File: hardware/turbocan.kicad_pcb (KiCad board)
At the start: 2 copper layers, 43 x 43 mm, 86 parts, among them J1 USB_C_Receptacle_USB2.0, J10 CAN_PORT, J11 FAN0, J12 FAN1, J13 HEAT, J14 PROBE, J2 STEPPER, J5 DEBUG, J7 ENDSTOPX, J8 ENDSTOPY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

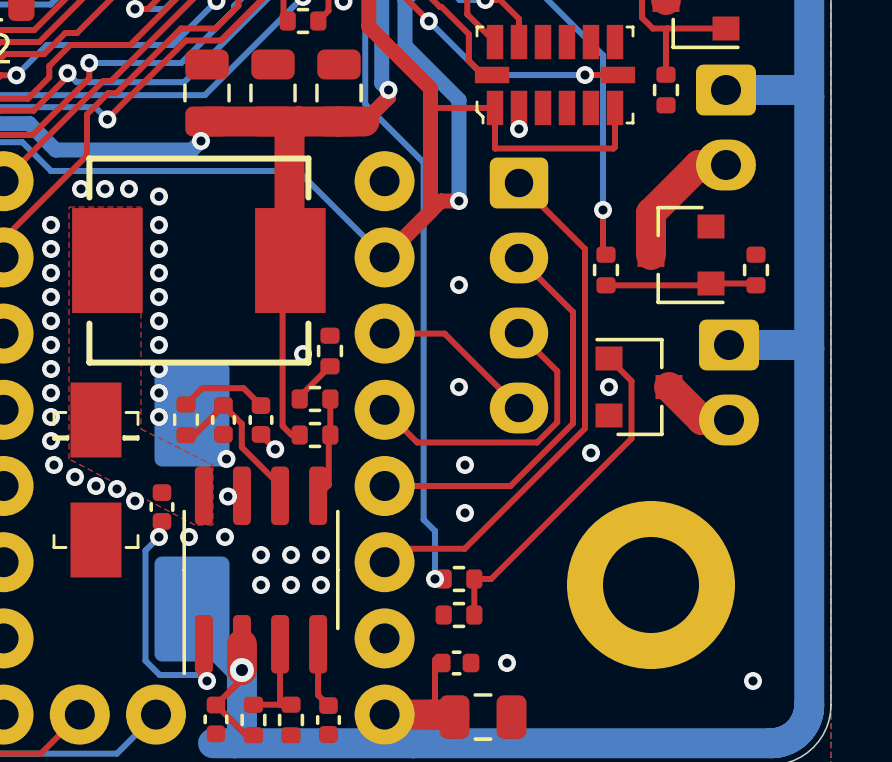
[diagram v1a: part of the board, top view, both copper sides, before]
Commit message: Replace heater mosfet
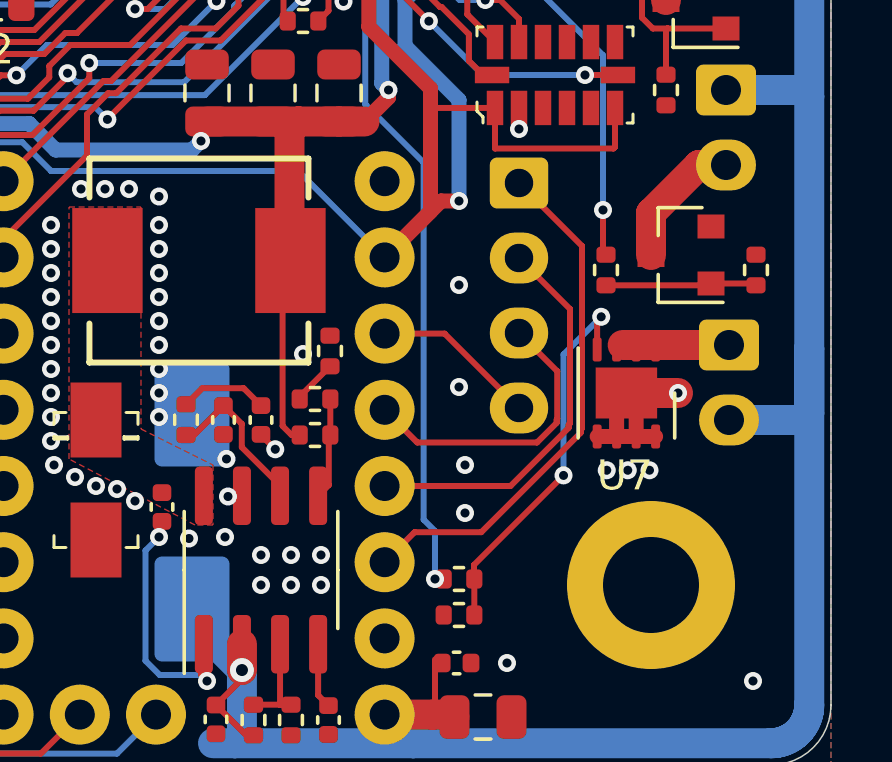
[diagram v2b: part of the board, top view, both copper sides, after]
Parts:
- U7: value AO3400A -> AON7400A; footprint Package_TO_SOT_SMD:SOT-23 -> turbocan:DFN-8-1EP_3x3mm_P0.65mm_EP1.7x2.05mm
- moved U7 0.47 mm to (50.2, 44.6), turned to 270 degrees
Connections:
- J1 pad A8: Net-(J1-PadA8) -> (no net)
- J1 pad B8: Net-(J1-PadB8) -> (no net)
- J13 pad 1: +24V -> Net-(J13-Pad1)
- J13 pad 2: Net-(J13-Pad2) -> +24V
- U3 pad 5: Net-(U3-Pad5) -> (no net)
- U7 pad 1: Net-(R16-Pad1) -> Net-(J13-Pad1)
- U7 pad 2: GND -> Net-(R16-Pad1)
- U7 pad 3: Net-(J13-Pad2) -> GND
- U8 pad 18: Net-(U8-Pad18) -> (no net)
- U8 pad 2: Net-(U8-Pad2) -> (no net)
- U8 pad 21: Net-(U8-Pad21) -> (no net)
- U8 pad 3: Net-(U8-Pad3) -> (no net)
- U8 pad 38: Net-(U8-Pad38) -> (no net)
- U8 pad 39: Net-(U8-Pad39) -> (no net)
- U8 pad 4: Net-(U8-Pad4) -> (no net)
- U9 pad 10: Net-(U9-Pad10) -> (no net)
- U9 pad 11: Net-(U9-Pad11) -> (no net)
- U9 pad 3: Net-(U9-Pad3) -> (no net)
- U9 pad 8: Net-(U9-Pad8) -> (no net)
- U9 pad 9: Net-(U9-Pad9) -> (no net)
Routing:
- net GND: track 28.0 -> 34.9 mm, vias 74 -> 76
- net Net-(J13-Pad1): track 0.00 -> 3.54 mm
- net Net-(J13-Pad2): track 2.46 -> 0.00 mm
- net +24V: track 185.1 -> 187.6 mm
- net Net-(R16-Pad1): track 11.4 -> 12.8 mm, vias 0 -> 2

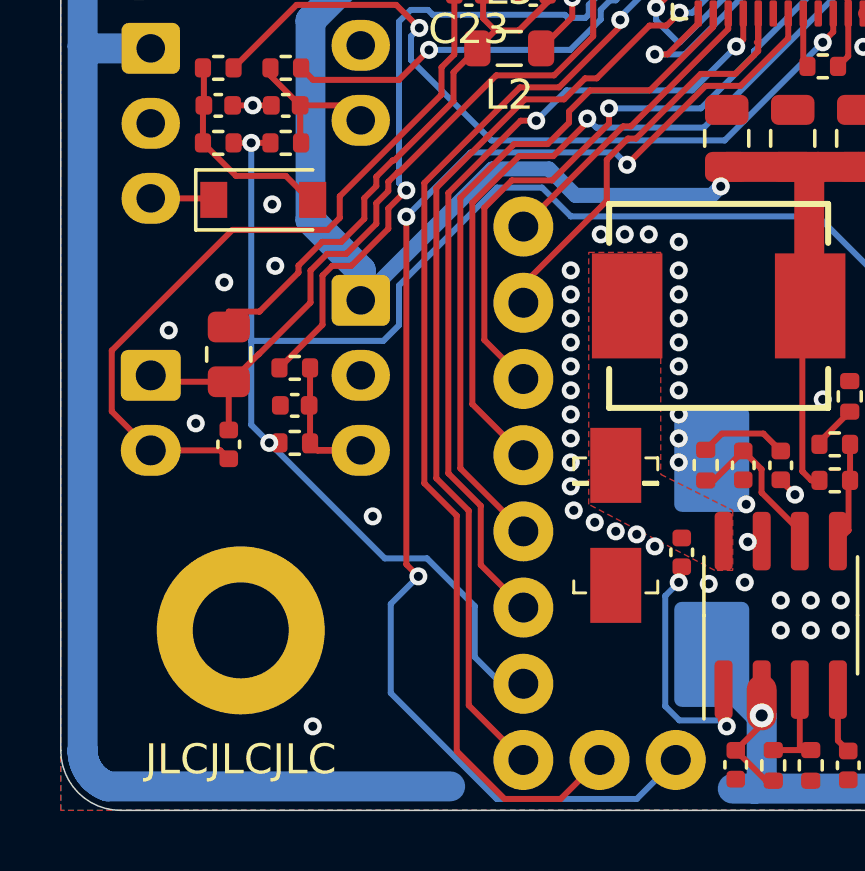
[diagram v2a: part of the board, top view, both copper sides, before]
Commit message: Replace pullup on MS1 with unpopulated resistor
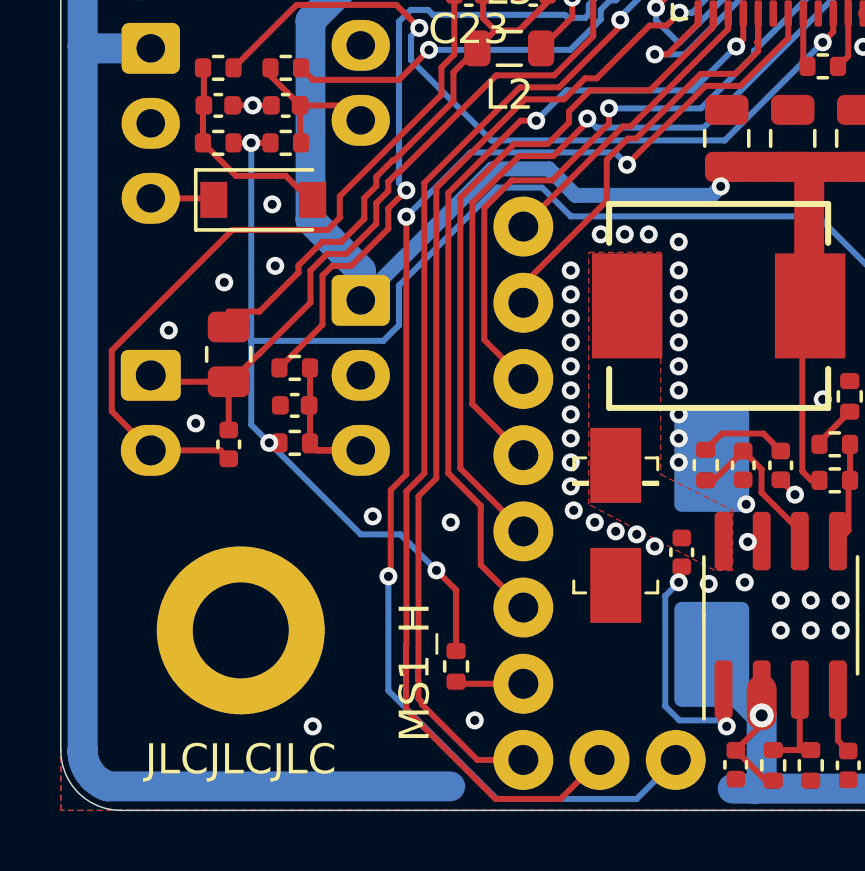
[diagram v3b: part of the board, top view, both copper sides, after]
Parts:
- added R29: DNP, Resistor_SMD:R_0402_1005Metric, F.Cu at (27.2, 52.2)
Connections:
- J1 pad A8: (no net) -> Net-(J1-PadA8)
- J1 pad B8: (no net) -> Net-(J1-PadB8)
- U2 pad 15: +3V3 -> Net-(R29-Pad2)
- U3 pad 5: (no net) -> Net-(U3-Pad5)
- U8 pad 18: (no net) -> Net-(U8-Pad18)
- U8 pad 2: (no net) -> Net-(U8-Pad2)
- U8 pad 21: (no net) -> Net-(U8-Pad21)
- U8 pad 3: (no net) -> Net-(U8-Pad3)
- U8 pad 38: (no net) -> Net-(U8-Pad38)
- U8 pad 39: (no net) -> Net-(U8-Pad39)
- U8 pad 4: (no net) -> Net-(U8-Pad4)
- U9 pad 10: (no net) -> Net-(U9-Pad10)
- U9 pad 11: (no net) -> Net-(U9-Pad11)
- U9 pad 3: (no net) -> Net-(U9-Pad3)
- U9 pad 8: (no net) -> Net-(U9-Pad8)
- U9 pad 9: (no net) -> Net-(U9-Pad9)
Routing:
- net +3V3: track 162.2 -> 159.7 mm, vias 13 -> 14
- net Net-(R29-Pad2): track 0.00 -> 2.27 mm
- net EN: track 41.9 -> 43.3 mm
- net DIAG: track 45.8 -> 46.5 mm
- net GND: vias 76 -> 78
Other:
- board text added: "MS1_H"

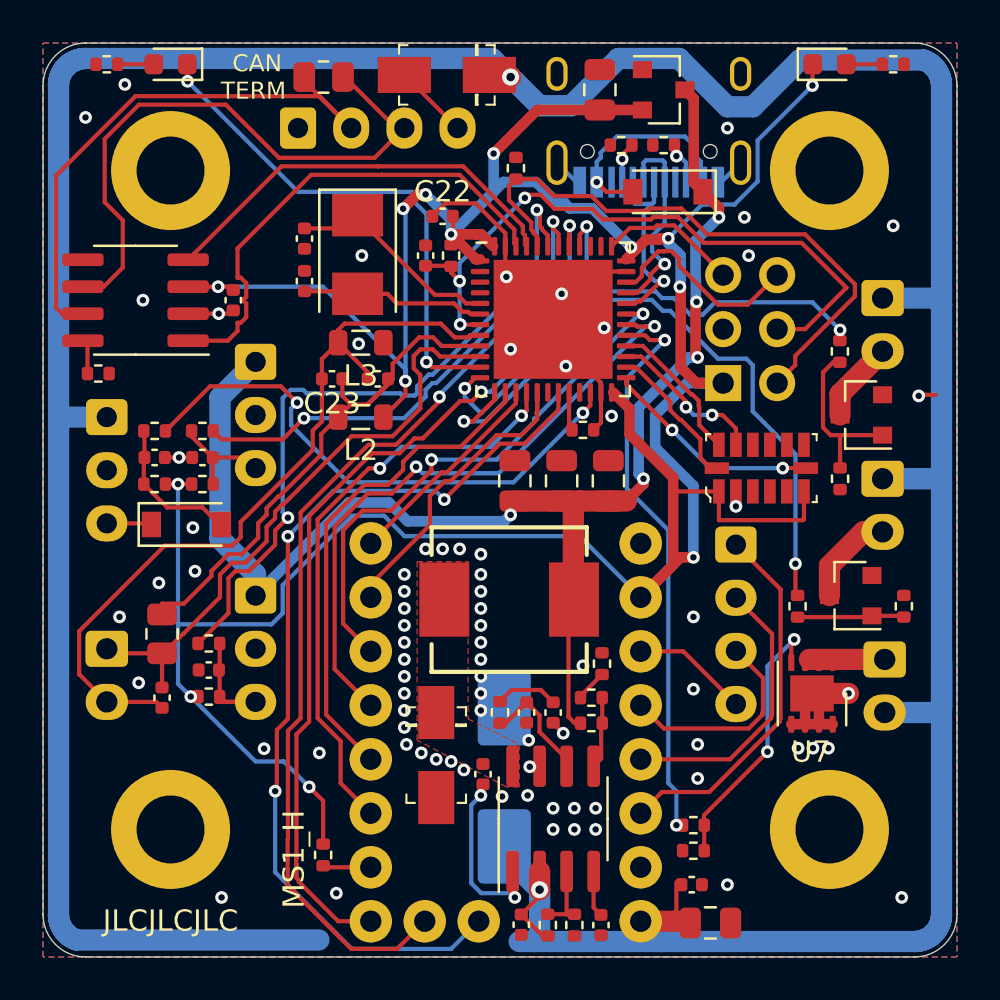
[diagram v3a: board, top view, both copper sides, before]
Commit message: Also add optional pullup resistors on MS2 and SPREAD
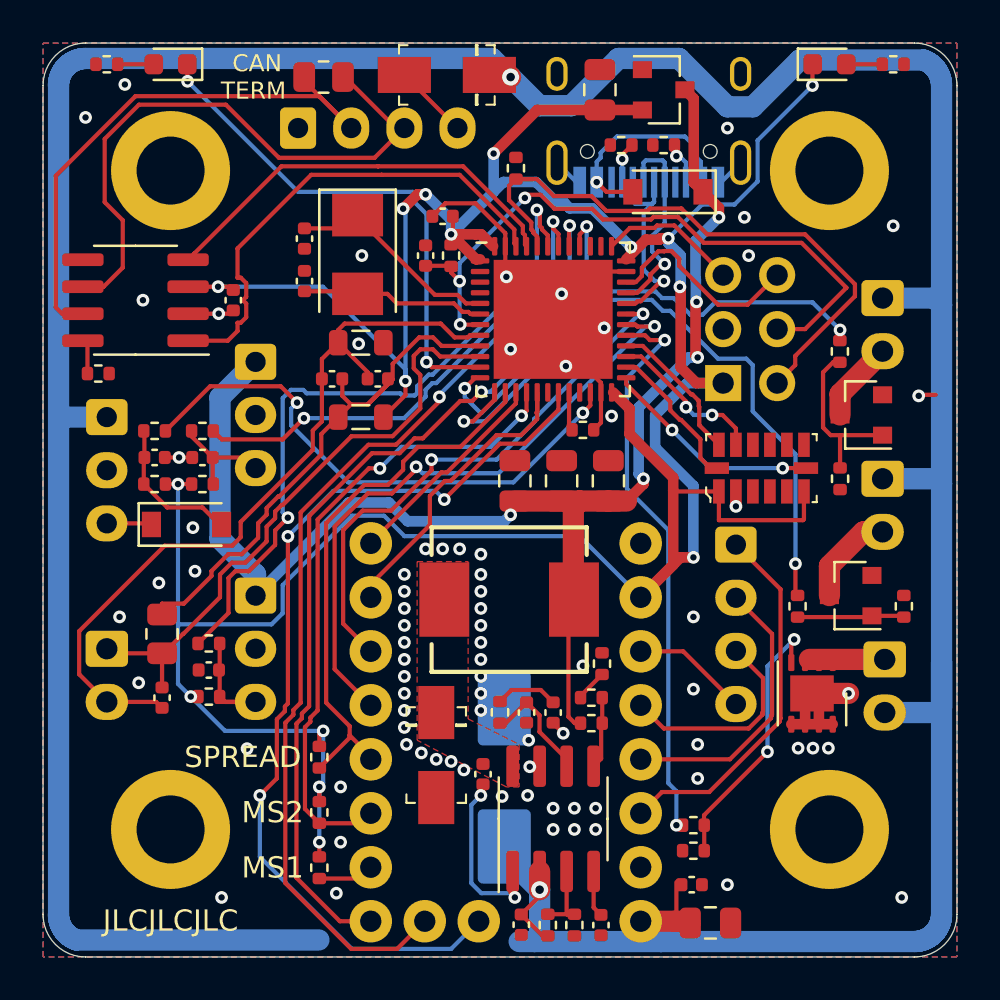
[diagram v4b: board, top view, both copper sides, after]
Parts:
- added R30: DNP, Resistor_SMD:R_0402_1005Metric, F.Cu at (27.0, 50.2)
- added R31: DNP, Resistor_SMD:R_0402_1005Metric, F.Cu at (27.0, 47.6)
- moved R29 0.63 mm to (27.0, 52.8)
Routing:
- net +3V3: track 159.7 -> 163.8 mm, vias 14 -> 16
- net MISO: track 27.7 -> 30.2 mm
- net INT2: track 23.4 -> 25.6 mm
- net INDEX: track 44.0 -> 44.6 mm
- net GND: vias 78 -> 79
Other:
- board text added: "MS1"
- board text added: "MS2"
- board text added: "SPREAD"
- board text removed: "MS1_H"

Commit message: Fix orientation of LEDs/C21 and update C8 to 1pF
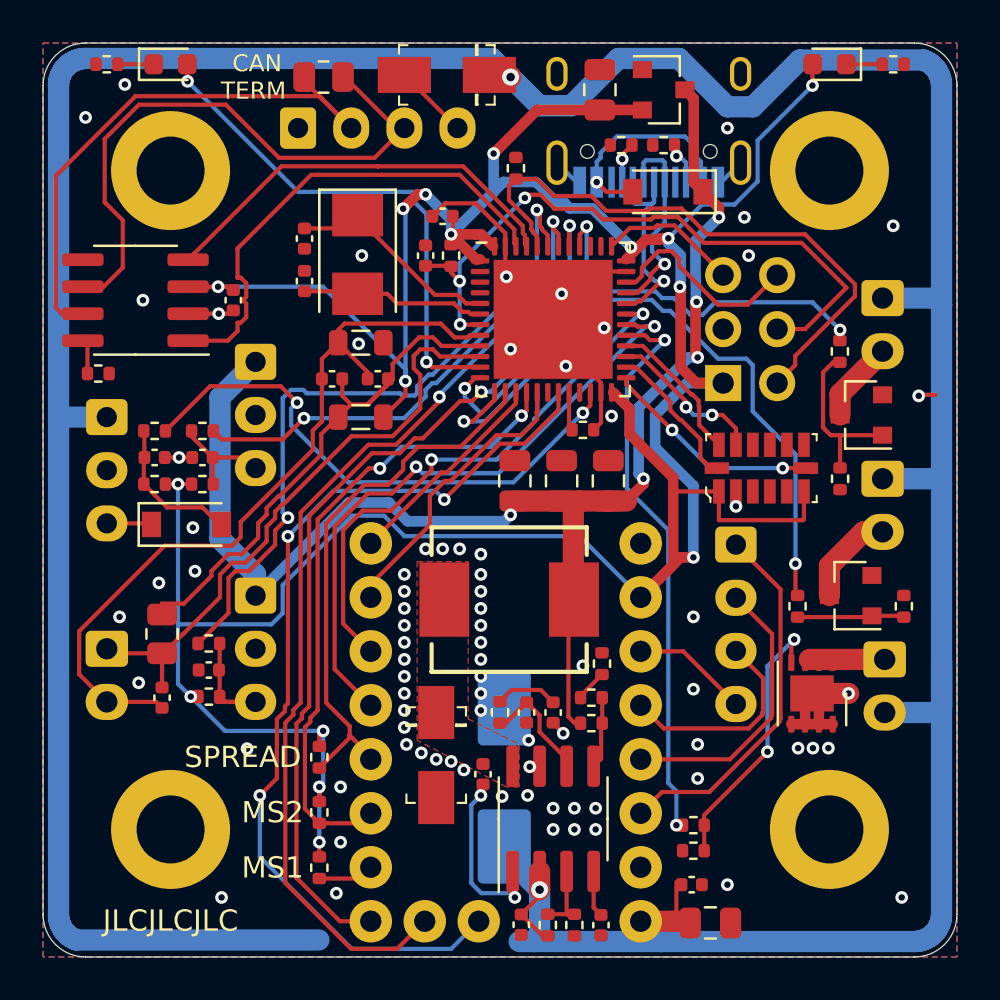
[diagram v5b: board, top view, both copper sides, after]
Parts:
- C8: value 6.8nF -> 1pF
- L1: value 10uH -> 6.8uH
- turned C21 to 90 degrees
- turned D5 to 0 degrees
- turned D6 to 180 degrees
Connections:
- C21 pad 1: GND -> +24V
- C21 pad 2: +24V -> GND
- D5 pad 1: LED -> Net-(D5-Pad1)
- D5 pad 2: Net-(D5-Pad2) -> LED
- D6 pad 1: +3V3 -> Net-(D6-Pad1)
- D6 pad 2: Net-(D6-Pad2) -> +3V3
- R23 pad 1: Net-(D5-Pad2) -> Net-(D5-Pad1)
- R24 pad 1: Net-(D6-Pad2) -> Net-(D6-Pad1)
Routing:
- net Net-(D6-Pad2): track 1.70 -> 0.00 mm
- net Net-(D6-Pad1): track 0.00 -> 1.70 mm
- net Net-(D5-Pad2): track 1.70 -> 0.00 mm
- net Net-(D5-Pad1): track 0.00 -> 1.70 mm

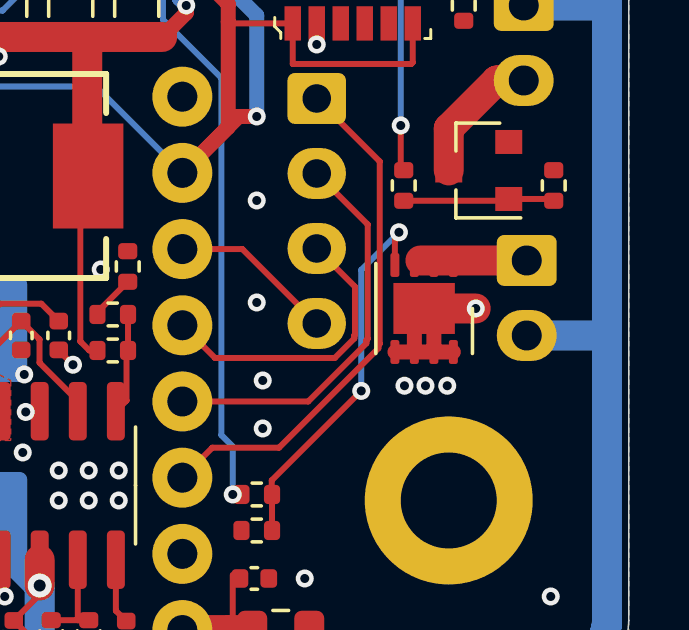
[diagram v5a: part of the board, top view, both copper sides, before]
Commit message: Swap drain and source on heater MOSFET.
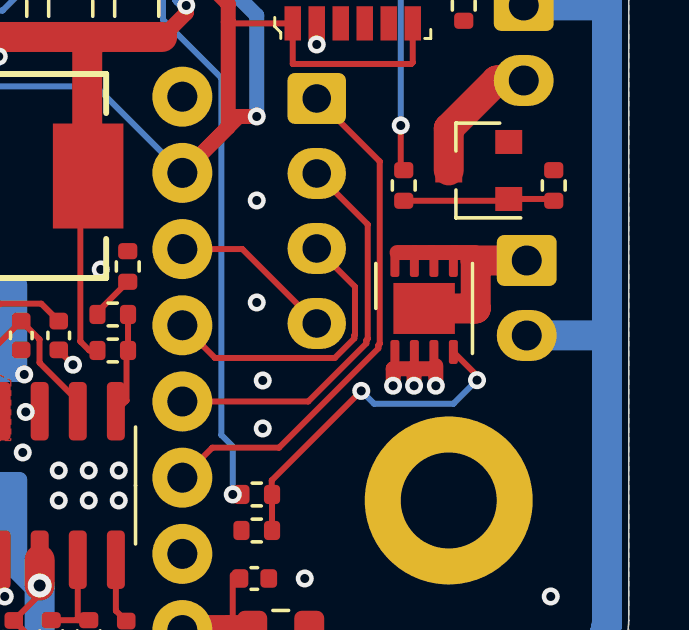
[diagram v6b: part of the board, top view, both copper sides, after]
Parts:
- removed REF**: VoronLogo, user:VoronLogo
- turned U7 to 90 degrees
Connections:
- J1 pad A8: Net-(J1-PadA8) -> (no net)
- J1 pad B8: Net-(J1-PadB8) -> (no net)
- U3 pad 5: Net-(U3-Pad5) -> (no net)
- U7 pad 1: Net-(J13-Pad1) -> GND
- U7 pad 3: GND -> Net-(J13-Pad1)
- U8 pad 18: Net-(U8-Pad18) -> (no net)
- U8 pad 2: Net-(U8-Pad2) -> (no net)
- U8 pad 21: Net-(U8-Pad21) -> (no net)
- U8 pad 3: Net-(U8-Pad3) -> (no net)
- U8 pad 38: Net-(U8-Pad38) -> (no net)
- U8 pad 39: Net-(U8-Pad39) -> (no net)
- U8 pad 4: Net-(U8-Pad4) -> (no net)
- U9 pad 10: Net-(U9-Pad10) -> (no net)
- U9 pad 11: Net-(U9-Pad11) -> (no net)
- U9 pad 3: Net-(U9-Pad3) -> (no net)
- U9 pad 8: Net-(U9-Pad8) -> (no net)
- U9 pad 9: Net-(U9-Pad9) -> (no net)
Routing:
- net Net-(J13-Pad1): track 3.54 -> 9.63 mm
- net GND: track 34.9 -> 31.8 mm, vias 79 -> 78
- net Net-(R16-Pad1): track 12.8 -> 11.5 mm

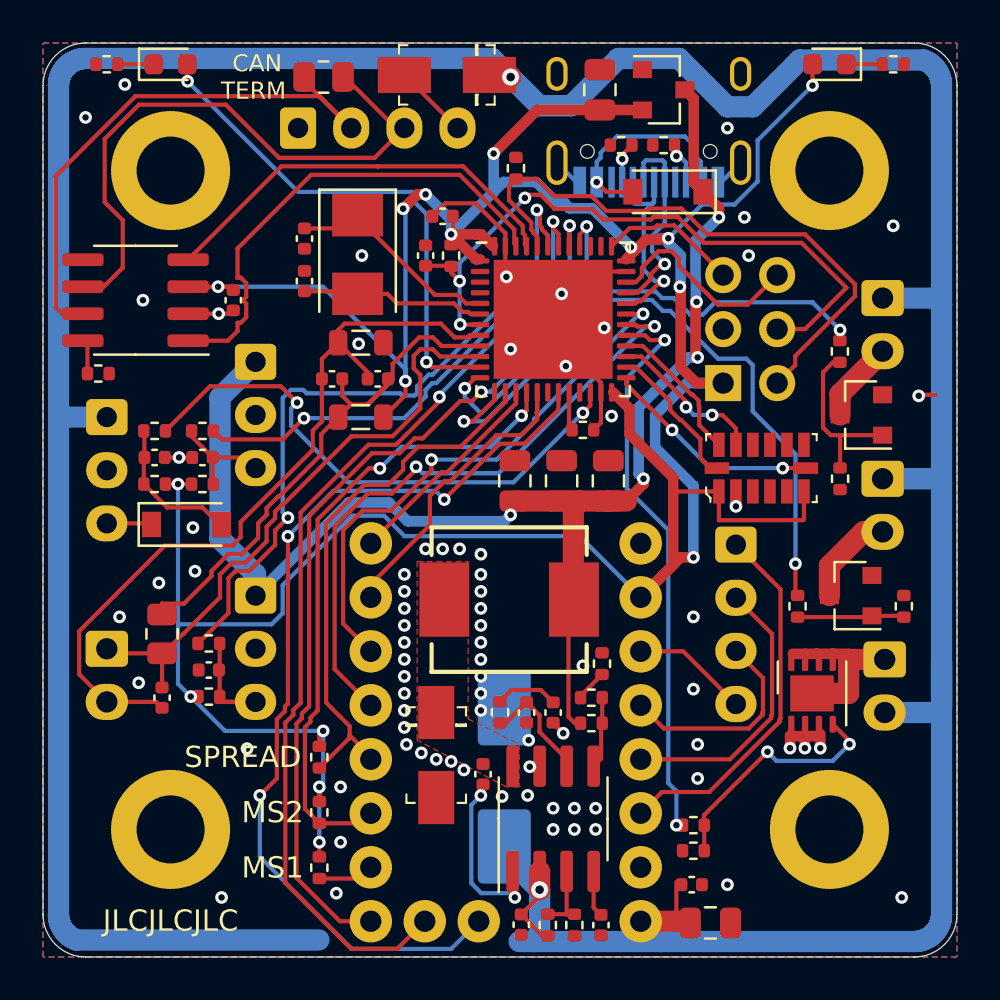
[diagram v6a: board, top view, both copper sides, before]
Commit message: Add thermal pad and vias for heater MOSFET.
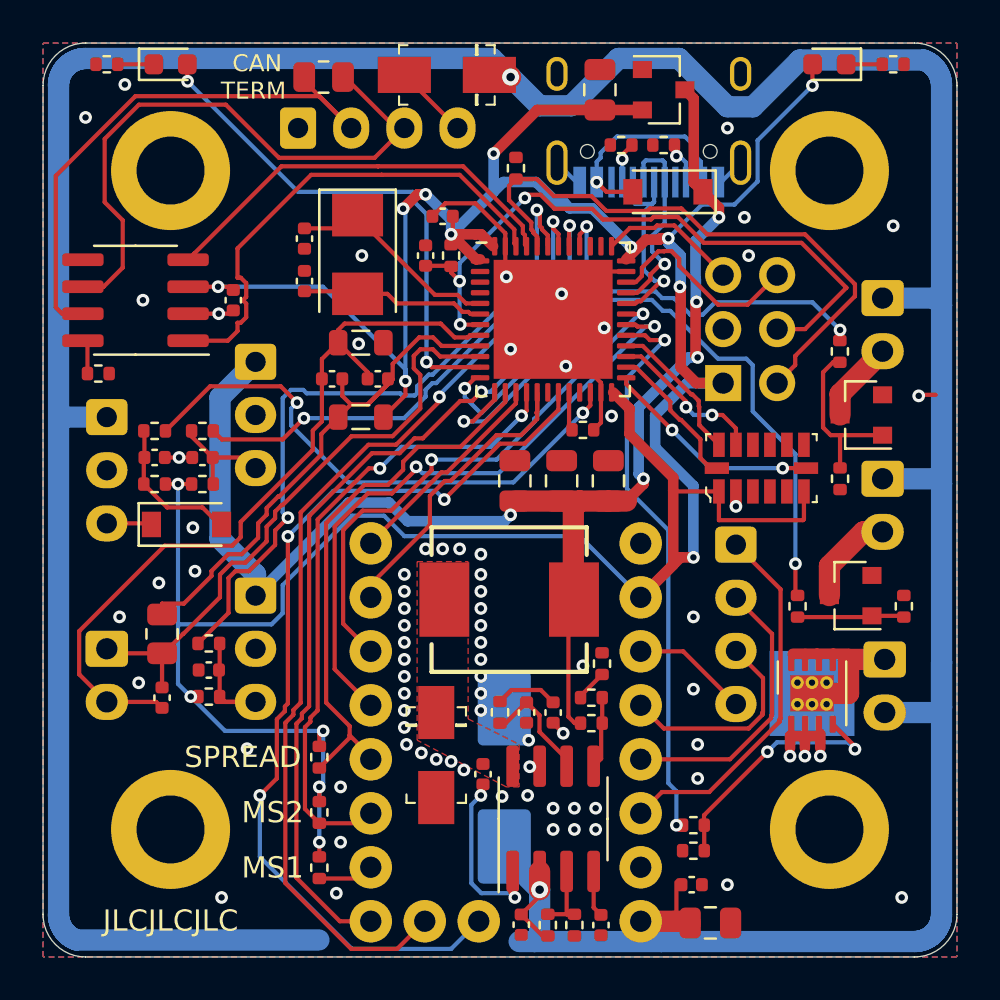
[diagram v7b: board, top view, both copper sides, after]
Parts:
- U7: footprint turbocan:DFN-8-1EP_3x3mm_P0.65mm_EP1.7x2.05mm -> turbocan:DFN-8-1EP_3x3mm_P0.65mm_EP1.7x2.05mm_Thermal_Pad
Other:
- rule trace_min: 0.2 -> 0
